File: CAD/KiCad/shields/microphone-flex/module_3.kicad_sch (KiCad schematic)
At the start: 1 part, among them J3 RIGHT / 1x05 RIGHT ANGLE

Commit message: Reroute microphone flex around the approved component placement
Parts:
- J3: footprint Shields:Flex_Socket_Side -> Shields:Flex_Socket_Right_Overhang
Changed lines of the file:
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@@
 (property "Reference" "J3" (at 101.6000 66.0400 0) (effects (font (size 1.016 1.016))  ))
 (property "Value" "RIGHT / 1x05 RIGHT ANGLE" (at 101.6000 68.5800 0) (effects (font (size 1.016 1.016))  ))
-(property "Footprint" "Shields:Flex_Socket_Side" (at 101.6000 83.8200 0) (effects (font (size 1.27 1.27))  (hide yes)))
+(property "Footprint" "Shields:Flex_Socket_Right_Overhang" (at 101.6000 83.8200 0) (effects (font (size 1.27 1.27))  (hide yes)))
 (property "Datasheet" "" (at 101.6000 83.8200 0) (effects (font (size 1.27 1.27))  (hide yes)))
 (property "Description" "Alternative socket; AR / Out / Gain / Vdd / GND in physical pad order. One module only." (at 101.6000 83.8200 0) (effects (font (size 1.27 1.27))  (hide yes)))

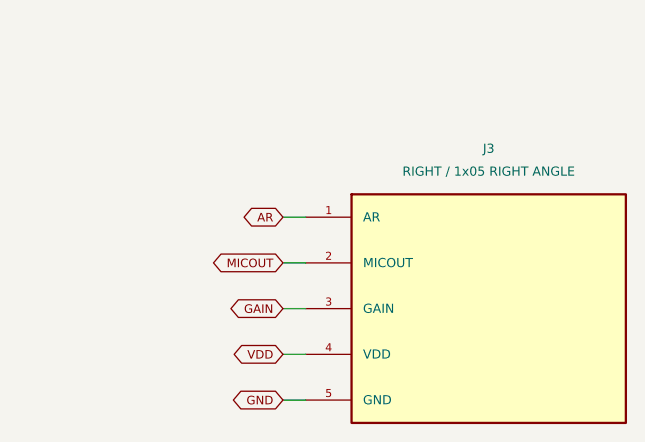
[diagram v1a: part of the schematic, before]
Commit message: Flip side microphones below the carrier and reverse their pin mapping
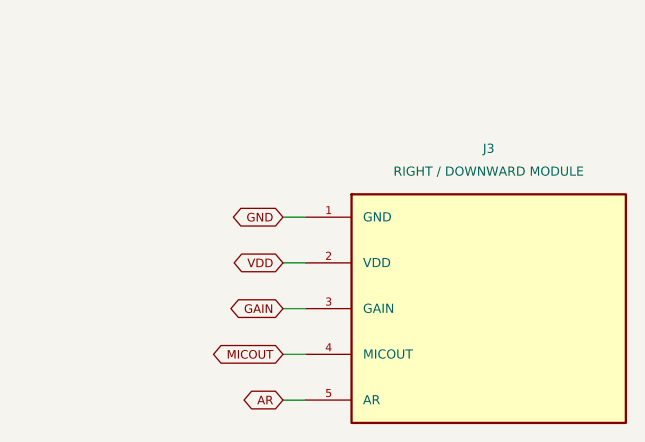
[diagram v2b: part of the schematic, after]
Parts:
- J3: value RIGHT / 1x05 RIGHT ANGLE -> RIGHT / DOWNWARD MODULE
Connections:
- net AR: now also J3.5 (AR); no longer J3.1 (AR)
- net GND: now also J3.1 (GND); no longer J3.5 (GND)
- net MICOUT: now also J3.4 (MICOUT); no longer J3.2 (MICOUT)
- net VDD: now also J3.2 (VDD); no longer J3.4 (VDD)
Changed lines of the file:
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@@
 (symbol (lib_id "Colloquy:J3") (at 101.6000 83.8200 0) (unit 1) (exclude_from_sim no) (in_bom yes) (on_board yes) (dnp no)
 (property "Reference" "J3" (at 101.6000 66.0400 0) (effects (font (size 1.016 1.016))  ))
-(property "Value" "RIGHT / 1x05 RIGHT ANGLE" (at 101.6000 68.5800 0) (effects (font (size 1.016 1.016))  ))
+(property "Value" "RIGHT / DOWNWARD MODULE" (at 101.6000 68.5800 0) (effects (font (size 1.016 1.016))  ))
 (property "Footprint" "Shields:Flex_Socket_Right_Overhang" (at 101.6000 83.8200 0) (effects (font (size 1.27 1.27))  (hide yes)))
 (property "Datasheet" "" (at 101.6000 83.8200 0) (effects (font (size 1.27 1.27))  (hide yes)))
-(property "Description" "Alternative socket; AR / Out / Gain / Vdd / GND in physical pad order. One module only." (at 101.6000 83.8200 0) (effects (font (size 1.27 1.27))  (hide yes)))
+(property "Description" "Side module hangs below the PCB, rotated 180 degrees about the insertion axis. GND / Vdd / Gain / Out / AR in physical pad order. One module only." (at 101.6000 83.8200 0) (effects (font (size 1.27 1.27))  (hide yes)))
 (pin "1")
 (pin "2")
@@
 (instances (project "microphone-flex" (path "/767eeb75-0bc5-5c78-a7ae-aa35b79c1dd4/a12f91a6-d5c6-5b04-b05b-0b13ecfaa013" (reference "J3") (unit 1)))))
 (wire (pts (xy 81.2800 73.6600) (xy 78.7400 73.6600)) (stroke (width 0) (type default)))
-(global_label "AR" (shape bidirectional) (at 78.7400 73.6600 180) (effects (font (size 0.95 0.95)) (justify right)) (property "Intersheetrefs" "${INTERSHEET_REFS}" (at 78.7400 73.6600 0) (effects (font (size 1.016 1.016))  (hide yes))))
+(global_label "GND" (shape bidirectional) (at 78.7400 73.6600 180) (effects (font (size 0.95 0.95)) (justify right)) (property "Intersheetrefs" "${INTERSHEET_REFS}" (at 78.7400 73.6600 0) (effects (font (size 1.016 1.016))  (hide yes))))
 (wire (pts (xy 81.2800 78.7400) (xy 78.7400 78.7400)) (stroke (width 0) (type default)))
-(global_label "MICOUT" (shape bidirectional) (at 78.7400 78.7400 180) (effects (font (size 0.95 0.95)) (justify right)) (property "Intersheetrefs" "${INTERSHEET_REFS}" (at 78.7400 78.7400 0) (effects (font (size 1.016 1.016))  (hide yes))))
+(global_label "VDD" (shape bidirectional) (at 78.7400 78.7400 180) (effects (font (size 0.95 0.95)) (justify right)) (property "Intersheetrefs" "${INTERSHEET_REFS}" (at 78.7400 78.7400 0) (effects (font (size 1.016 1.016))  (hide yes))))
 (wire (pts (xy 81.2800 83.8200) (xy 78.7400 83.8200)) (stroke (width 0) (type default)))
 (global_label "GAIN" (shape bidirectional) (at 78.7400 83.8200 180) (effects (font (size 0.95 0.95)) (justify right)) (property "Intersheetrefs" "${INTERSHEET_REFS}" (at 78.7400 83.8200 0) (effects (font (size 1.016 1.016))  (hide yes))))
 (wire (pts (xy 81.2800 88.9000) (xy 78.7400 88.9000)) (stroke (width 0) (type default)))
-(global_label "VDD" (shape bidirectional) (at 78.7400 88.9000 180) (effects (font (size 0.95 0.95)) (justify right)) (property "Intersheetrefs" "${INTERSHEET_REFS}" (at 78.7400 88.9000 0) (effects (font (size 1.016 1.016))  (hide yes))))
+(global_label "MICOUT" (shape bidirectional) (at 78.7400 88.9000 180) (effects (font (size 0.95 0.95)) (justify right)) (property "Intersheetrefs" "${INTERSHEET_REFS}" (at 78.7400 88.9000 0) (effects (font (size 1.016 1.016))  (hide yes))))
 (wire (pts (xy 81.2800 93.9800) (xy 78.7400 93.9800)) (stroke (width 0) (type default)))
-(global_label "GND" (shape bidirectional) (at 78.7400 93.9800 180) (effects (font (size 0.95 0.95)) (justify right)) (property "Intersheetrefs" "${INTERSHEET_REFS}" (at 78.7400 93.9800 0) (effects (font (size 1.016 1.016))  (hide yes))))
+(global_label "AR" (shape bidirectional) (at 78.7400 93.9800 180) (effects (font (size 0.95 0.95)) (justify right)) (property "Intersheetrefs" "${INTERSHEET_REFS}" (at 78.7400 93.9800 0) (effects (font (size 1.016 1.016))  (hide yes))))
           (embedded_fonts no))
